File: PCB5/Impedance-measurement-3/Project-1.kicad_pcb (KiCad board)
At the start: 2 copper layers, 103.5 x 74.5 mm, 81 parts, among them J2 USB_C_Receptacle, U1 STM32F303CCT6, U2 W25Q32JVSSIQ, U5 TS 2940 CZ33, U9 OPA4141AID

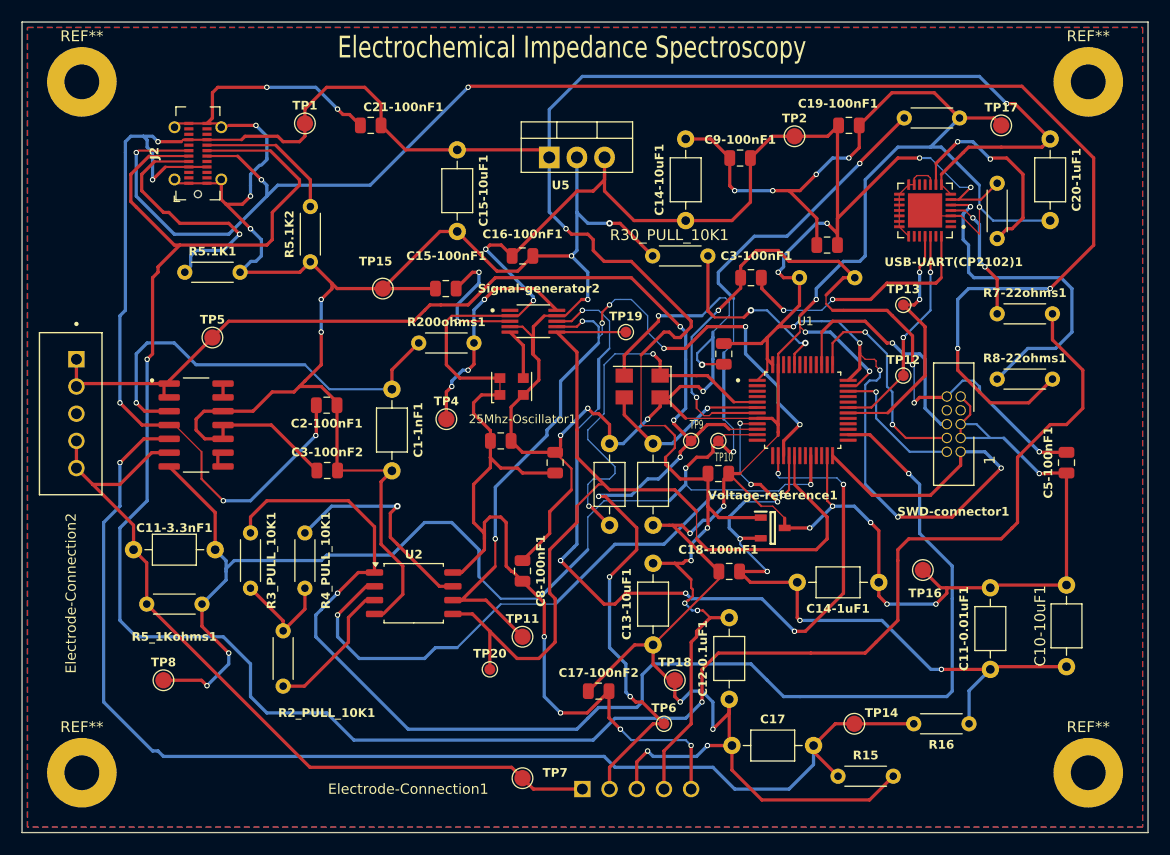
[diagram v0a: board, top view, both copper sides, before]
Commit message: Led removed 9/8/2026
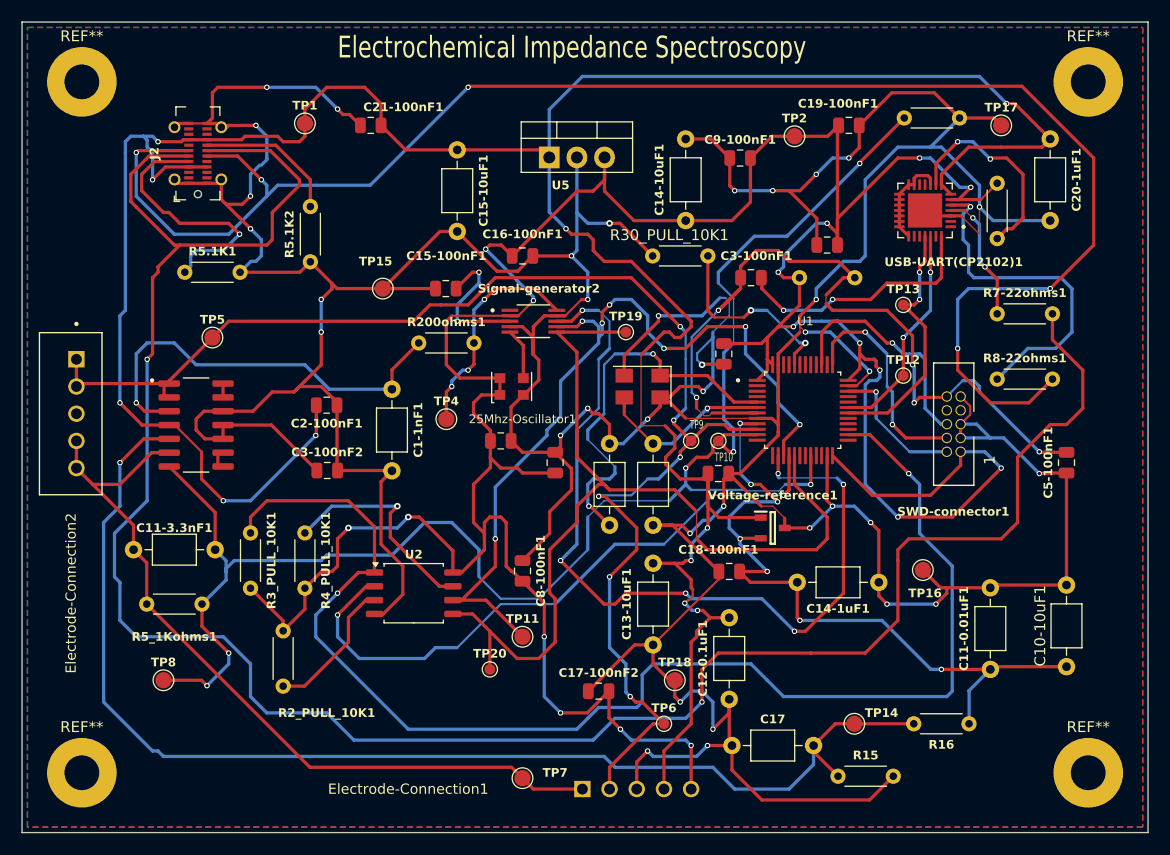
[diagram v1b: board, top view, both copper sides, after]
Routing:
- net VDD: track 281.1 -> 302.2 mm, vias 15 -> 17
